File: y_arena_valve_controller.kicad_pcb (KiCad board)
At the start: 2 copper layers, 74.9 x 90.2 mm, 20 parts, among them P1 PWR_JACK_2.1x5.5_SMD_VERT

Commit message: Add parts to BOM
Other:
- board text added: "0"
- board text added: "1"
- board text added: "2"
- board text added: "MANIFOLD"
- board text added: "RELAY 0"
- board text added: "RELAY 1"
- board text added: "RELAY 2"
- board text added: "RELAY 3"
- board text added: "RELAY 4"
- board text added: "RELAY 5"
- board text added: "RELAY 6"
- board text added: "RELAY 7"
- board text added: "RELAY 8"
- board text added: "VALVE"
- board text added: "y_arena_valve_controller Janelia Research Campus 07/22/2020 ver 1.1"
- board text removed: "y_arena_valve_controller Janelia Research Campus 07/20/2020 ver 1.1"

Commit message: Updated parts
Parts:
- removed PHIDGET1: PHIDGET_RELAY_16X_COMP, y_arena_valve_controller:PHIDGET_RELAY_16X_COMP
- added C10: 1uF, valve_spike_hold:SM0805_POL_L, F.Cu at (239.8, 115.6)
- added C11: 15nF, valve_spike_hold:SM0402, F.Cu at (243.1, 116.7)
- added C12: 1uF, valve_spike_hold:SM0805_POL_L, F.Cu at (289.8, 73.9)
- added C13: 15nF, valve_spike_hold:SM0402, F.Cu at (298.6, 70.8)
- added C14: 1uF, valve_spike_hold:SM0805_POL_L, F.Cu at (268.0, 101.0)
- added C15: 15nF, valve_spike_hold:SM0402, F.Cu at (276.8, 97.9)
- added C16: 1uF, valve_spike_hold:SM0805_POL_L, F.Cu at (289.8, 87.5)
- added C17: 15nF, valve_spike_hold:SM0402, F.Cu at (293.1, 88.6)
- added C18: 1uF, valve_spike_hold:SM0805_POL_L, F.Cu at (261.6, 115.6)
- added C19: 15nF, valve_spike_hold:SM0402, F.Cu at (270.4, 112.4)
- added C2: 1uF, valve_spike_hold:SM0805_POL_L, F.Cu at (196.3, 115.6)
- added C3: 15nF, valve_spike_hold:SM0402, F.Cu at (199.6, 116.7)
- added C4: 1uF, valve_spike_hold:SM0805_POL_L, F.Cu at (268.0, 73.9)
- added C5: 15nF, valve_spike_hold:SM0402, F.Cu at (274.9, 70.8)
- added C6: 1uF, valve_spike_hold:SM0805_POL_L, F.Cu at (218.0, 115.6)
- added C7: 15nF, valve_spike_hold:SM0402, F.Cu at (226.9, 112.4)
- added C8: 1uF, valve_spike_hold:SM0805_POL_L, F.Cu at (268.0, 87.5)
- added C9: 15nF, valve_spike_hold:SM0402, F.Cu at (276.8, 84.3)
- added D10: DIODE_SCHOTTKY_20V_1A, valve_spike_hold:SM0805_POL, F.Cu at (267.7, 90.6)
- added D11: DIODE_LOW_REV_CURRENT, valve_spike_hold:SOD-123, F.Cu at (240.1, 112.5)
- added D12: DIODE_SCHOTTKY_20V_1A, valve_spike_hold:SM0805_POL, F.Cu at (239.5, 118.7)
- added D13: DIODE_LOW_REV_CURRENT, valve_spike_hold:SOD-123, F.Cu at (290.1, 70.9)
- added D14: DIODE_SCHOTTKY_20V_1A, valve_spike_hold:SM0805_POL, F.Cu at (289.5, 77.1)
- added D15: DIODE_LOW_REV_CURRENT, valve_spike_hold:SOD-123, F.Cu at (268.3, 98.0)
- added D16: DIODE_SCHOTTKY_20V_1A, valve_spike_hold:SM0805_POL, F.Cu at (267.7, 104.2)
- added D17: DIODE_LOW_REV_CURRENT, valve_spike_hold:SOD-123, F.Cu at (290.1, 84.4)
- added D18: DIODE_SCHOTTKY_20V_1A, valve_spike_hold:SM0805_POL, F.Cu at (289.5, 90.6)
- added D19: DIODE_LOW_REV_CURRENT, valve_spike_hold:SOD-123, F.Cu at (261.9, 112.5)
- added D2: DIODE_LOW_REV_CURRENT, y_arena_valve_controller:SOD-123, F.Cu at (215.7, 70.9)
- added D20: DIODE_SCHOTTKY_20V_1A, valve_spike_hold:SM0805_POL, F.Cu at (261.3, 118.7)
- added D3: DIODE_LOW_REV_CURRENT, valve_spike_hold:SOD-123, F.Cu at (196.6, 112.5)
- added D4: DIODE_SCHOTTKY_20V_1A, valve_spike_hold:SM0805_POL, F.Cu at (196.0, 118.7)
- added D5: DIODE_LOW_REV_CURRENT, valve_spike_hold:SOD-123, F.Cu at (268.3, 70.9)
- added D6: DIODE_SCHOTTKY_20V_1A, valve_spike_hold:SM0805_POL, F.Cu at (267.7, 77.1)
- added D7: DIODE_LOW_REV_CURRENT, valve_spike_hold:SOD-123, F.Cu at (218.3, 112.5)
- added D8: DIODE_SCHOTTKY_20V_1A, valve_spike_hold:SM0805_POL, F.Cu at (217.8, 118.7)
- added D9: DIODE_LOW_REV_CURRENT, valve_spike_hold:SOD-123, F.Cu at (268.3, 84.4)
- added L1: LED_GRN, y_arena_valve_controller:LED0805, F.Cu at (220.5, 70.5)
- added L10: LED_GRN, valve_spike_hold:LED0805, F.Cu at (254.9, 120.1)
- added L2: LED_GRN, valve_spike_hold:LED0805, F.Cu at (83.8, 165.1)
- added L3: LED_GRN, valve_spike_hold:LED0805, F.Cu at (261.3, 78.5)
- added L4: LED_GRN, valve_spike_hold:LED0805, F.Cu at (211.4, 120.1)
- added L5: LED_GRN, valve_spike_hold:LED0805, F.Cu at (261.3, 92.0)
- added L6: LED_GRN, valve_spike_hold:LED0805, F.Cu at (233.2, 120.1)
- added L7: LED_GRN, valve_spike_hold:LED0805, F.Cu at (283.1, 78.5)
- added L8: LED_GRN, valve_spike_hold:LED0805, F.Cu at (261.3, 105.6)
- added L9: LED_GRN, valve_spike_hold:LED0805, F.Cu at (283.1, 92.0)
- added R1: 499, y_arena_valve_controller:SM0805, F.Cu at (224.2, 71.5)
- added R10: 205k, valve_spike_hold:SM0402, F.Cu at (221.4, 116.7)
- added R11: 499, valve_spike_hold:SM0805, F.Cu at (272.4, 85.0)
- added R12: 150k, valve_spike_hold:SM0402, F.Cu at (271.3, 88.6)
- added R13: 205k, valve_spike_hold:SM0402, F.Cu at (274.9, 84.3)
- added R14: 499, valve_spike_hold:SM0805, F.Cu at (244.2, 113.1)
- added R15: 150k, valve_spike_hold:SM0402, F.Cu at (246.7, 112.4)
- added R16: 205k, valve_spike_hold:SM0402, F.Cu at (248.7, 112.4)
- added R17: 499, valve_spike_hold:SM0805, F.Cu at (294.2, 71.5)
- added R18: 150k, valve_spike_hold:SM0402, F.Cu at (293.1, 75.0)
- added R19: 205k, valve_spike_hold:SM0402, F.Cu at (296.6, 70.8)
- added R2: 499, valve_spike_hold:SM0805, F.Cu at (200.7, 113.1)
- added R20: 499, valve_spike_hold:SM0805, F.Cu at (272.4, 98.6)
- added R21: 150k, valve_spike_hold:SM0402, F.Cu at (271.3, 102.1)
- added R22: 205k, valve_spike_hold:SM0402, F.Cu at (274.9, 97.9)
- added R23: 499, valve_spike_hold:SM0805, F.Cu at (294.2, 85.0)
- added R24: 150k, valve_spike_hold:SM0402, F.Cu at (298.6, 84.3)
- added R25: 205k, valve_spike_hold:SM0402, F.Cu at (296.6, 84.3)
- added R26: 499, valve_spike_hold:SM0805, F.Cu at (266.0, 113.1)
- added R27: 150k, valve_spike_hold:SM0402, F.Cu at (264.9, 116.7)
- added R28: 205k, valve_spike_hold:SM0402, F.Cu at (268.5, 112.4)
- added R3: 150k, valve_spike_hold:SM0402, F.Cu at (203.2, 112.4)
- added R4: 205k, valve_spike_hold:SM0402, F.Cu at (205.1, 112.4)
- added R5: 499, valve_spike_hold:SM0805, F.Cu at (272.4, 71.5)
- added R6: 150k, valve_spike_hold:SM0402, F.Cu at (271.3, 75.0)
- added R7: 205k, valve_spike_hold:SM0402, F.Cu at (276.8, 70.8)
- added R8: 499, valve_spike_hold:SM0805, F.Cu at (222.5, 113.1)
- added R9: 150k, valve_spike_hold:SM0402, F.Cu at (224.9, 112.4)
- added SW1: SPST_SLIDE_AS, y_arena_valve_controller:SPST_SLIDE_AS, F.Cu at (88.3, 137.8)
- added TEENSY1: TEENSY_4.0, y_arena_valve_controller:TEENSY_4.0, F.Cu at (64.1, 121.9)
- added U1: DRV103, valve_spike_hold:SOIC_8, F.Cu at (190.7, 115.0)
- added U2: DRV103, valve_spike_hold:SOIC_8, F.Cu at (262.4, 73.3)
- added U3: DRV103, valve_spike_hold:SOIC_8, F.Cu at (212.5, 115.0)
- added U4: DRV103, valve_spike_hold:SOIC_8, F.Cu at (262.4, 86.9)
- added U5: DRV103, valve_spike_hold:SOIC_8, F.Cu at (234.2, 115.0)
- added U6: DRV103, valve_spike_hold:SOIC_8, F.Cu at (284.2, 73.3)
- added U7: DRV103, valve_spike_hold:SOIC_8, F.Cu at (262.4, 100.4)
- added U8: DRV103, valve_spike_hold:SOIC_8, F.Cu at (284.2, 86.9)
- added U9: DRV103, valve_spike_hold:SOIC_8, F.Cu at (256.0, 115.0)
- S1, S2, S3, S4, S5, S6, S7, S8, S9: value VAL** -> LEECO_LHDB; footprint y_arena_valve_controller:LEECO_LHDB -> valve_spike_hold:LEECO_LHDB
- moved C1 33.7 mm to (116.8, 111.1)
- moved D1 24.2 mm to (112.4, 111.1)
- moved P1 24.1 mm to (112.4, 126.4)
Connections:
- S1 pad 2: /VALVE_0 -> /valve_0/SH
- S2 pad 2: /VALVE_1 -> /valve_1/SH
- S3 pad 2: /VALVE_2 -> /valve_2/SH
- S4 pad 2: /VALVE_3 -> /valve_3/SH
- S5 pad 2: /VALVE_4 -> /valve_4/SH
- S6 pad 2: /VALVE_5 -> /valve_5/SH
- S7 pad 2: /VALVE_6 -> /valve_6/SH
- S8 pad 2: /VALVE_7 -> /valve_7/SH
- S9 pad 2: /VALVE_8 -> /valve_8/SH
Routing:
- net VCC: track 145.4 -> 0.00 mm
- net GND: track 122.1 -> 0.00 mm
- net /VALVE_2: track 73.6 -> 0.00 mm
- net /VALVE_1: track 71.1 -> 0.00 mm
- net /VALVE_0: track 68.5 -> 0.00 mm
- net /VALVE_4: track 52.5 -> 0.00 mm
- net /VALVE_5: track 52.3 -> 0.00 mm
- net /VALVE_3: track 47.9 -> 0.00 mm
- net /VALVE_7: track 46.7 -> 0.00 mm
- net /VALVE_6: track 44.9 -> 0.00 mm
- net /VALVE_8: track 44.4 -> 0.00 mm
- net VAA: track 8.70 -> 0.00 mm
- removed copper zone on B.Cu, net GND
- removed copper zone on F.Cu, net VCC
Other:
- board text added: "ARM"
- board text added: "y_arena_valve_controller Janelia Research Campus 07/31/2020 ver 1.2"
- board text removed: "MANIFOLD"
- board text removed: "RELAY 0"
- board text removed: "RELAY 1"
- board text removed: "RELAY 2"
- board text removed: "RELAY 3"
- board text removed: "RELAY 4"
- board text removed: "RELAY 5"
- board text removed: "RELAY 6"
- board text removed: "RELAY 7"
- board text removed: "RELAY 8"
- board text removed: "y_arena_valve_controller Janelia Research Campus 07/22/2020 ver 1.1"

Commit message: Use 0402 parts instead of 0805
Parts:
- C10, C12, C14, C16, C18, C8: footprint valve_spike_hold:SM0805_POL_L -> valve_spike_hold:SM0402_POL
- C2, C4, C6: footprint valve_spike_hold:SM0805_POL_L -> valve_spike_hold:SM0402_POL; moved to B.Cu
- C3, C5, C7, R10, R3, R4, R6, R7, R9, U1, U2, U3: moved to B.Cu
- D10, D12, D14, D16, D18, D20: value DIODE_SCHOTTKY_20V_1A -> DIODE_SCHOTTKY_0402; footprint valve_spike_hold:SM0805_POL -> valve_spike_hold:SM0402_POL
- D11, D13, D15, D17, D19, D3, D5, D7, D9: value DIODE_LOW_REV_CURRENT -> DIODE_LOW_REV_CURRENT_0402; footprint valve_spike_hold:SOD-123 -> valve_spike_hold:SM0402_POL; moved to B.Cu
- D2: value DIODE_LOW_REV_CURRENT -> DIODE_LOW_REV_CURRENT_0402; footprint y_arena_valve_controller:SOD-123 -> y_arena_valve_controller:SM0402_POL; moved to B.Cu
- D4, D6, D8: value DIODE_SCHOTTKY_20V_1A -> DIODE_SCHOTTKY_0402; footprint valve_spike_hold:SM0805_POL -> valve_spike_hold:SM0402_POL; moved to B.Cu
- R1: value 499 -> 390; footprint y_arena_valve_controller:SM0805 -> y_arena_valve_controller:SM0402; moved to B.Cu
- R11, R14, R17, R2, R20, R23, R26, R5, R8: value 499 -> 390; footprint valve_spike_hold:SM0805 -> valve_spike_hold:SM0402; moved to B.Cu
- SW1: value SPST_SLIDE_AS -> SLIDE_SWITCH_AS_SPST
- moved R17 209.0 mm to (89.5, 113.7), turned to 180 degrees
- moved D13 207.5 mm to (87.0, 113.7), turned to 180 degrees
- moved D6 205.6 mm to (62.2, 71.8), turned to 180 degrees
- moved R7 204.5 mm to (72.4, 73.0), turned to 270 degrees
- moved C5 202.5 mm to (72.4, 70.5), turned to 270 degrees
- moved R23 202.4 mm to (94.6, 118.7), turned to 180 degrees
- moved C4 201.3 mm to (66.7, 74.3), turned to 270 degrees
- moved D17 200.9 mm to (92.1, 118.7), turned to 180 degrees
- moved R6 199.0 mm to (72.4, 67.9), turned to 270 degrees
- moved L7 198.0 mm to (88.3, 113.7), turned to 90 degrees
- moved U2 195.8 mm to (66.7, 70.5), turned to 270 degrees
- moved R5 193.8 mm to (84.5, 118.7), turned to 180 degrees
- moved D5 192.4 mm to (81.9, 118.7), turned to 180 degrees
- moved L9 191.6 mm to (93.3, 118.7), turned to 90 degrees
- moved R11 187.0 mm to (89.5, 123.8), turned to 180 degrees
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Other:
- board size 74.9 x 90.2 mm -> 74.9 x 82.6 mm
- board text added: "ARM 0"
- board text added: "ARM 1"
- board text added: "ARM 2"
- board text added: "VALVE 0"
- board text added: "VALVE 1"
- board text added: "VALVE 2"

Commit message: Ready to route
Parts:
- C10, C11, C12, C13, C14, C15, C16, C17, C18, C19, C8, C9, D10, D12, D14, D16, D18, D20, R12, R13, R15, R16, R18, R19, R21, R22, R24, R25, R27, R28, U4, U5, U6, U7, U8, U9: moved to B.Cu
- P1: value PWR_JACK_2.1x5.5_SMD_VERT -> PWR_JACK_2.1x5.5; footprint y_arena_valve_controller:DCJACK_3PIN_SMD_VERT -> y_arena_valve_controller:DCJACK_2PIN_HIGHCURRENT
- SW1: value SLIDE_SWITCH_AS_SPST -> SPST_SLIDE_AS
- moved D14 205.6 mm to (84.5, 61.6), turned to 180 degrees
- moved C13 202.9 mm to (95.9, 62.9), turned to 270 degrees
- moved R19 200.8 mm to (95.9, 65.4), turned to 270 degrees
- moved C12 199.7 mm to (90.2, 66.7), turned to 270 degrees
- moved R18 197.7 mm to (95.9, 60.3), turned to 270 degrees
- moved U6 194.3 mm to (90.2, 62.9), turned to 270 degrees
- moved D10 183.8 mm to (84.5, 76.8), turned to 180 degrees
- moved C9 181.1 mm to (95.9, 78.1), turned to 270 degrees
- moved R13 179.0 mm to (95.9, 80.6), turned to 270 degrees
- moved D18 178.4 mm to (112.4, 69.2), turned to 180 degrees
- moved C8 177.9 mm to (90.2, 81.9), turned to 270 degrees
- moved R12 175.9 mm to (95.9, 75.6), turned to 270 degrees
- moved R24 175.6 mm to (123.8, 67.9), turned to 270 degrees
- moved R25 173.2 mm to (123.8, 73.0), turned to 270 degrees
- moved U4 172.5 mm to (90.2, 78.1), turned to 270 degrees
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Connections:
- S1 pad 1: VCC -> /valve_0/SH
- S1 pad 2: /valve_0/SH -> VCC
- S2 pad 1: VCC -> /valve_1/SH
- S2 pad 2: /valve_1/SH -> VCC
- S3 pad 1: VCC -> /valve_2/SH
- S3 pad 2: /valve_2/SH -> VCC
- S4 pad 1: VCC -> /valve_3/SH
- S4 pad 2: /valve_3/SH -> VCC
- S5 pad 1: VCC -> /valve_4/SH
- S5 pad 2: /valve_4/SH -> VCC
- S6 pad 1: VCC -> /valve_5/SH
- S6 pad 2: /valve_5/SH -> VCC
- S7 pad 1: VCC -> /valve_6/SH
- S7 pad 2: /valve_6/SH -> VCC
- S8 pad 1: VCC -> /valve_7/SH
- S8 pad 2: /valve_7/SH -> VCC
- S9 pad 1: VCC -> /valve_8/SH
- S9 pad 2: /valve_8/SH -> VCC
- TEENSY1 pad 0: /VALVE_0 -> (no net)
- TEENSY1 pad 1: /VALVE_1 -> (no net)
- TEENSY1 pad 14: (no net) -> /VALVE_8
- TEENSY1 pad 15: (no net) -> /VALVE_7
- TEENSY1 pad 16: (no net) -> /VALVE_6
- TEENSY1 pad 17: (no net) -> /VALVE_5
- TEENSY1 pad 18: (no net) -> /VALVE_4
- TEENSY1 pad 19: (no net) -> /VALVE_3
- TEENSY1 pad 2: /VALVE_2 -> (no net)
- TEENSY1 pad 20: (no net) -> /VALVE_2
- TEENSY1 pad 21: (no net) -> /VALVE_1
- TEENSY1 pad 22: (no net) -> /VALVE_0
- TEENSY1 pad 3: /VALVE_3 -> (no net)
- TEENSY1 pad 4: /VALVE_4 -> (no net)
- TEENSY1 pad 5: /VALVE_5 -> (no net)
- TEENSY1 pad 6: /VALVE_6 -> (no net)
- TEENSY1 pad 7: /VALVE_7 -> (no net)
- TEENSY1 pad 8: /VALVE_8 -> (no net)
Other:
- board size 74.9 x 82.6 mm -> 74.9 x 80.6 mm

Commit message: Route tracks and zones
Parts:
- MH1, MH2, MH3: value MOUNTING_HOLE_4-40 -> VAL**
- S1, S2, S3, S4, S5, S6, S7, S8, S9: value LEECO_LHDB -> VAL**
- SW1: value SPST_SLIDE_AS -> SLIDE_SWITCH_AS_SPST
- turned C7 to 270 degrees
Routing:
- net GND: track 0.00 -> 288.6 mm, vias 0 -> 1
- net VCC: track 0.00 -> 283.1 mm
- net /VALVE_1: track 0.00 -> 85.2 mm
- net /valve_0/SH: track 0.00 -> 73.8 mm
- net /VALVE_0: track 0.00 -> 73.1 mm, vias 0 -> 1
- net /VALVE_2: track 0.00 -> 71.4 mm, vias 0 -> 2
- net /valve_2/SH: track 0.00 -> 68.9 mm
- net /valve_1/SH: track 0.00 -> 66.7 mm
- net /valve_8/SH: track 0.00 -> 62.6 mm
- net /valve_7/SH: track 0.00 -> 60.4 mm
- net /valve_5/SH: track 0.00 -> 59.4 mm
- net /Vled: track 0.00 -> 58.9 mm
- net /valve_6/SH: track 0.00 -> 57.9 mm
- net /valve_4/SH: track 0.00 -> 56.9 mm
- net /valve_3/SH: track 0.00 -> 54.4 mm
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- added copper zone on B.Cu, net GND
- added copper zone on F.Cu, net VCC
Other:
- net class POWER added: clearance 0.1016, trace_width 0.4064, via_dia 0.889, via_drill 0.635
- net class SUPERPOWER removed

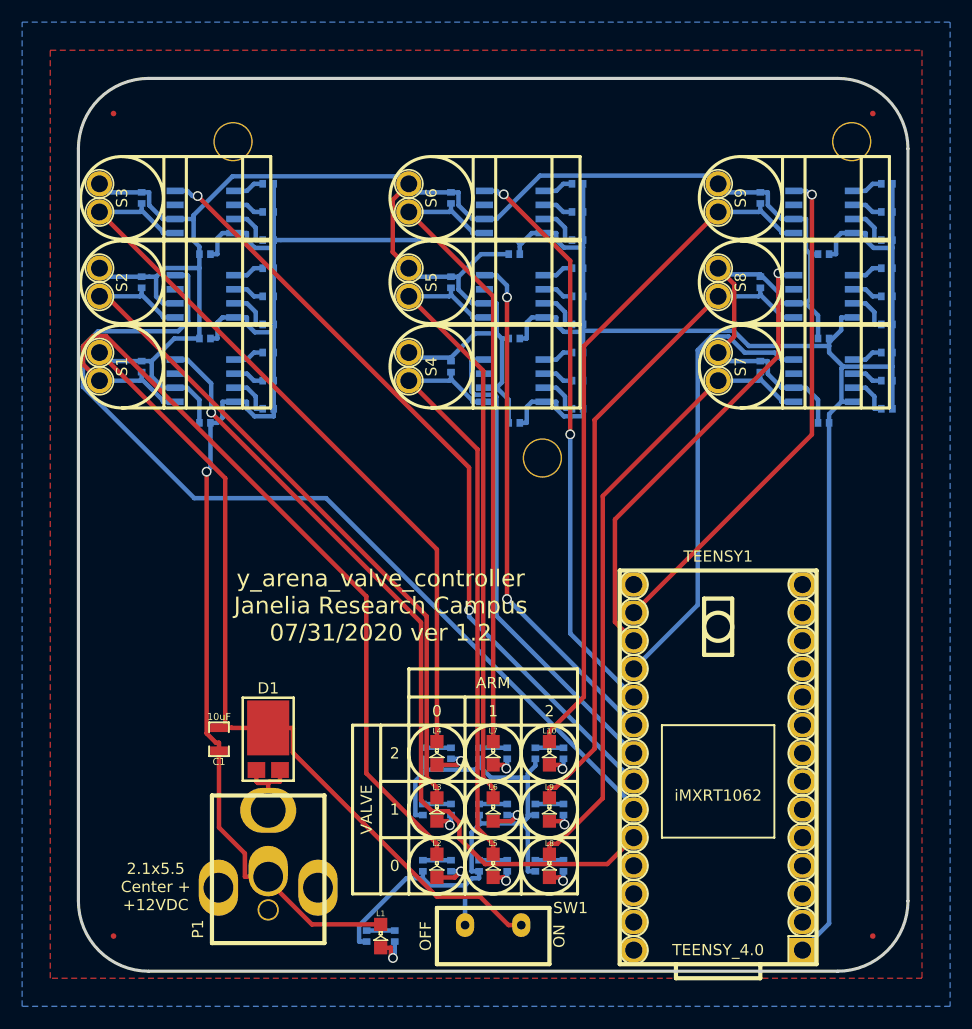
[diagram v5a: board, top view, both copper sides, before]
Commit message: Use surface mount slide switch and barrel jack
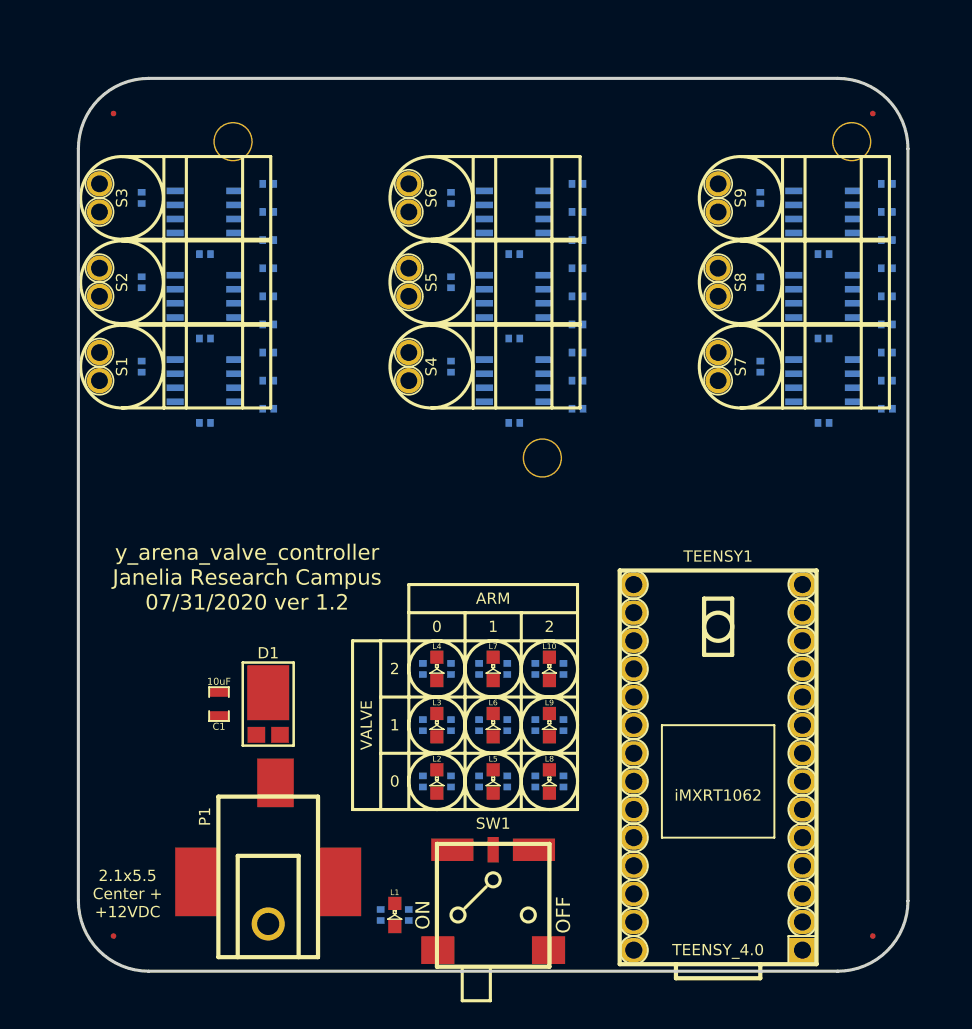
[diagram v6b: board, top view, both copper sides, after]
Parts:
- P1: value PWR_JACK_2.1x5.5 -> PWR_JACK_2.1x5.5_SMD_RA; footprint y_arena_valve_controller:DCJACK_2PIN_HIGHCURRENT -> y_arena_valve_controller:DCJACK_3PAD_SMD_RA
- SW1: value SLIDE_SWITCH_AS_SPST -> SPDT_SLIDE_500A_SM; footprint y_arena_valve_controller:SPST_SLIDE_AS -> y_arena_valve_controller:SPDT_SLIDE_500A_SM
- moved D11 7.62 mm to (87.0, 109.2)
- moved D13 7.62 mm to (87.0, 104.1)
- moved D15 7.62 mm to (92.1, 114.3)
- moved D17 7.62 mm to (92.1, 109.2)
- moved D19 7.62 mm to (92.1, 104.1)
- moved D3 7.62 mm to (81.9, 114.3)
- moved D5 7.62 mm to (81.9, 109.2)
- moved D7 7.62 mm to (81.9, 104.1)
- moved D9 7.62 mm to (87.0, 114.3)
- moved L10 7.62 mm to (93.3, 104.1), turned to 0 degrees
- moved L2 7.62 mm to (83.2, 114.3), turned to 0 degrees
- moved L3 7.62 mm to (83.2, 109.2), turned to 0 degrees
- moved L4 7.62 mm to (83.2, 104.1), turned to 0 degrees
- moved L5 7.62 mm to (88.3, 114.3), turned to 0 degrees
- moved L6 7.62 mm to (88.3, 109.2), turned to 0 degrees
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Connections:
- SW1 pad 1: VCC -> /Vled
- SW1 pad 3: /Vled -> (no net)
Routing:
- net GND: track 288.6 -> 0.00 mm, vias 1 -> 0
- net VCC: track 283.1 -> 0.00 mm
- net /VALVE_1: track 85.2 -> 0.00 mm
- net /valve_0/SH: track 73.8 -> 0.00 mm
- net /VALVE_0: track 73.1 -> 0.00 mm, vias 1 -> 0
- net /VALVE_2: track 71.4 -> 0.00 mm, vias 2 -> 0
- net /valve_2/SH: track 68.9 -> 0.00 mm
- net /valve_1/SH: track 66.7 -> 0.00 mm
- net /valve_8/SH: track 62.6 -> 0.00 mm
- net /valve_7/SH: track 60.4 -> 0.00 mm
- net /valve_5/SH: track 59.4 -> 0.00 mm
- net /Vled: track 58.9 -> 0.00 mm
- net /valve_6/SH: track 57.9 -> 0.00 mm
- net /valve_4/SH: track 56.9 -> 0.00 mm
- net /valve_3/SH: track 54.4 -> 0.00 mm
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- removed copper zone on B.Cu, net GND
- removed copper zone on F.Cu, net VCC

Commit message: Finished routing
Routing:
- net GND: track 0.00 -> 300.6 mm, vias 0 -> 1
- net VCC: track 0.00 -> 286.7 mm
- net /VALVE_2: track 0.00 -> 94.7 mm
- net /VALVE_1: track 0.00 -> 73.0 mm, vias 0 -> 1
- net /VALVE_0: track 0.00 -> 68.3 mm, vias 0 -> 1
- net /valve_0/SH: track 0.00 -> 66.2 mm
- net /VALVE_5: track 0.00 -> 64.0 mm
- net /Vled: track 0.00 -> 63.4 mm, vias 0 -> 1
- net /valve_2/SH: track 0.00 -> 61.2 mm
- net /VALVE_4: track 0.00 -> 59.6 mm, vias 0 -> 1
- net /valve_1/SH: track 0.00 -> 58.7 mm
- net /valve_8/SH: track 0.00 -> 55.0 mm
- net /VALVE_3: track 0.00 -> 53.1 mm, vias 0 -> 1
- net /valve_7/SH: track 0.00 -> 52.7 mm
- net /valve_5/SH: track 0.00 -> 51.8 mm
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- added copper zone on B.Cu, net GND
- added copper zone on F.Cu, net VCC
